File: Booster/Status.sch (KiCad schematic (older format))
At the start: 33 parts, among them J601 StatusLED, P601 ~OVERCURRENT_OUT, P602 ~OVERCURRENT_OUT_OP, P603 MSTR_SW, P604 MSTR_SW_OUT, P605 MSTR_SW_OUT_OP, P606 DRIVER_ENABLE_OUT_OP, P607 DRIVER_ENABLE_OUT, Q604 BC817-40, SW601 MSTR_SW, U601 74HC00, U602 PC817, U603 PC817, U604 PC817

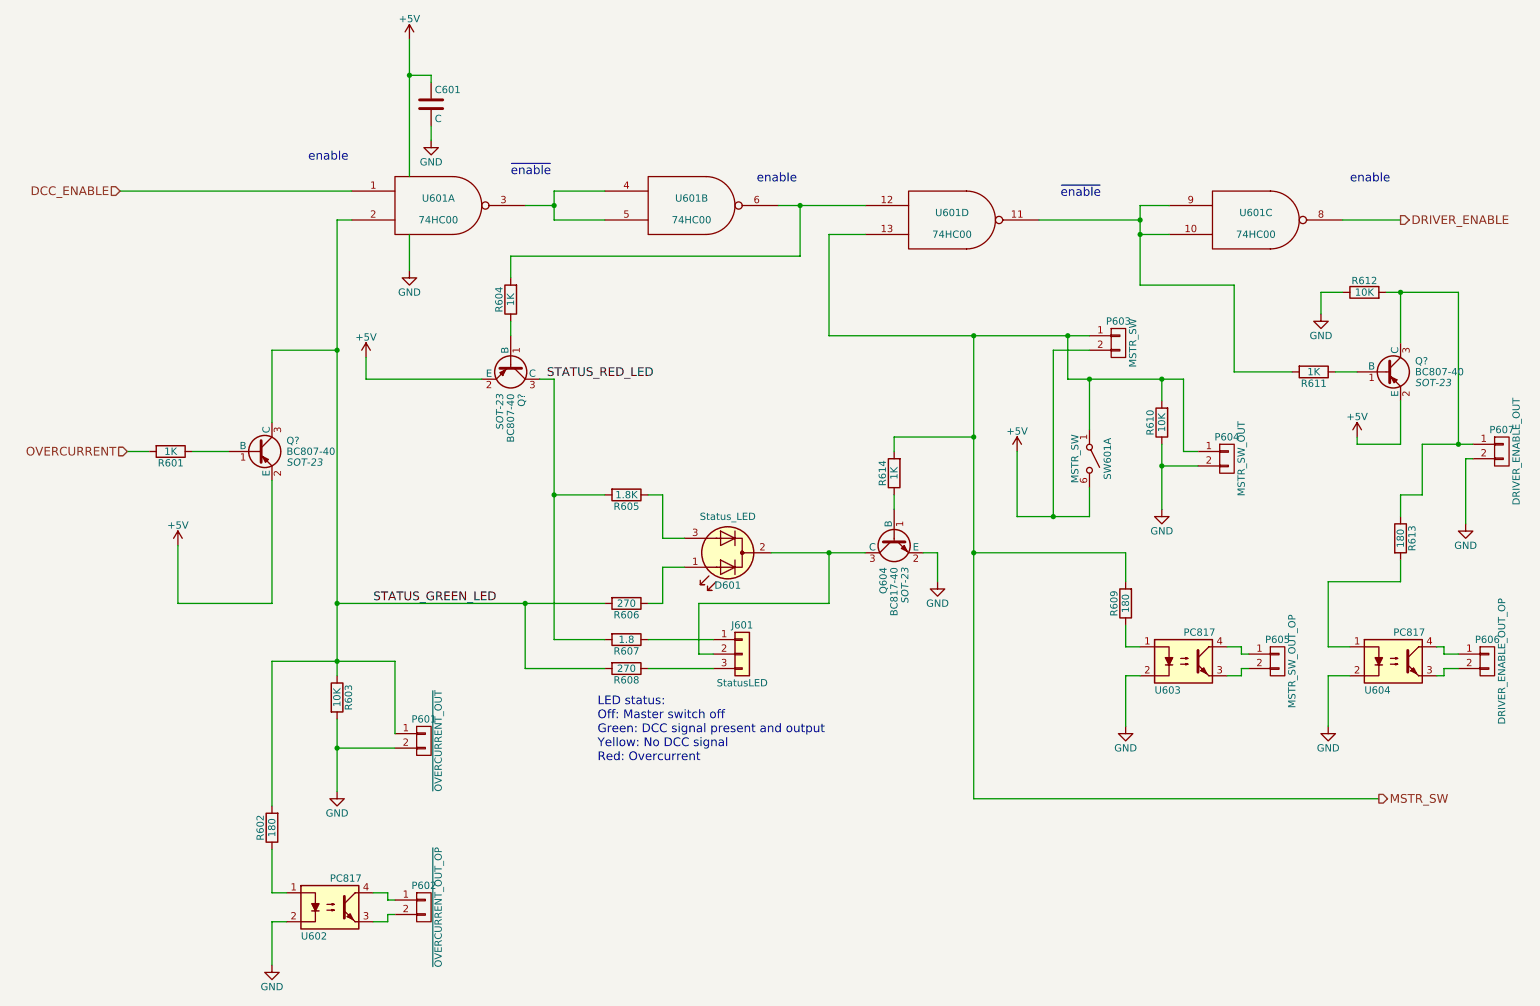
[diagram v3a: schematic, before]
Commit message: Replaced NAND gate with AND as the additional NOT gates ended up only used to negate the NAND gates directly. One extra AND gate used to allow resetting overcurrent by either master switch or DCC disable/enable.
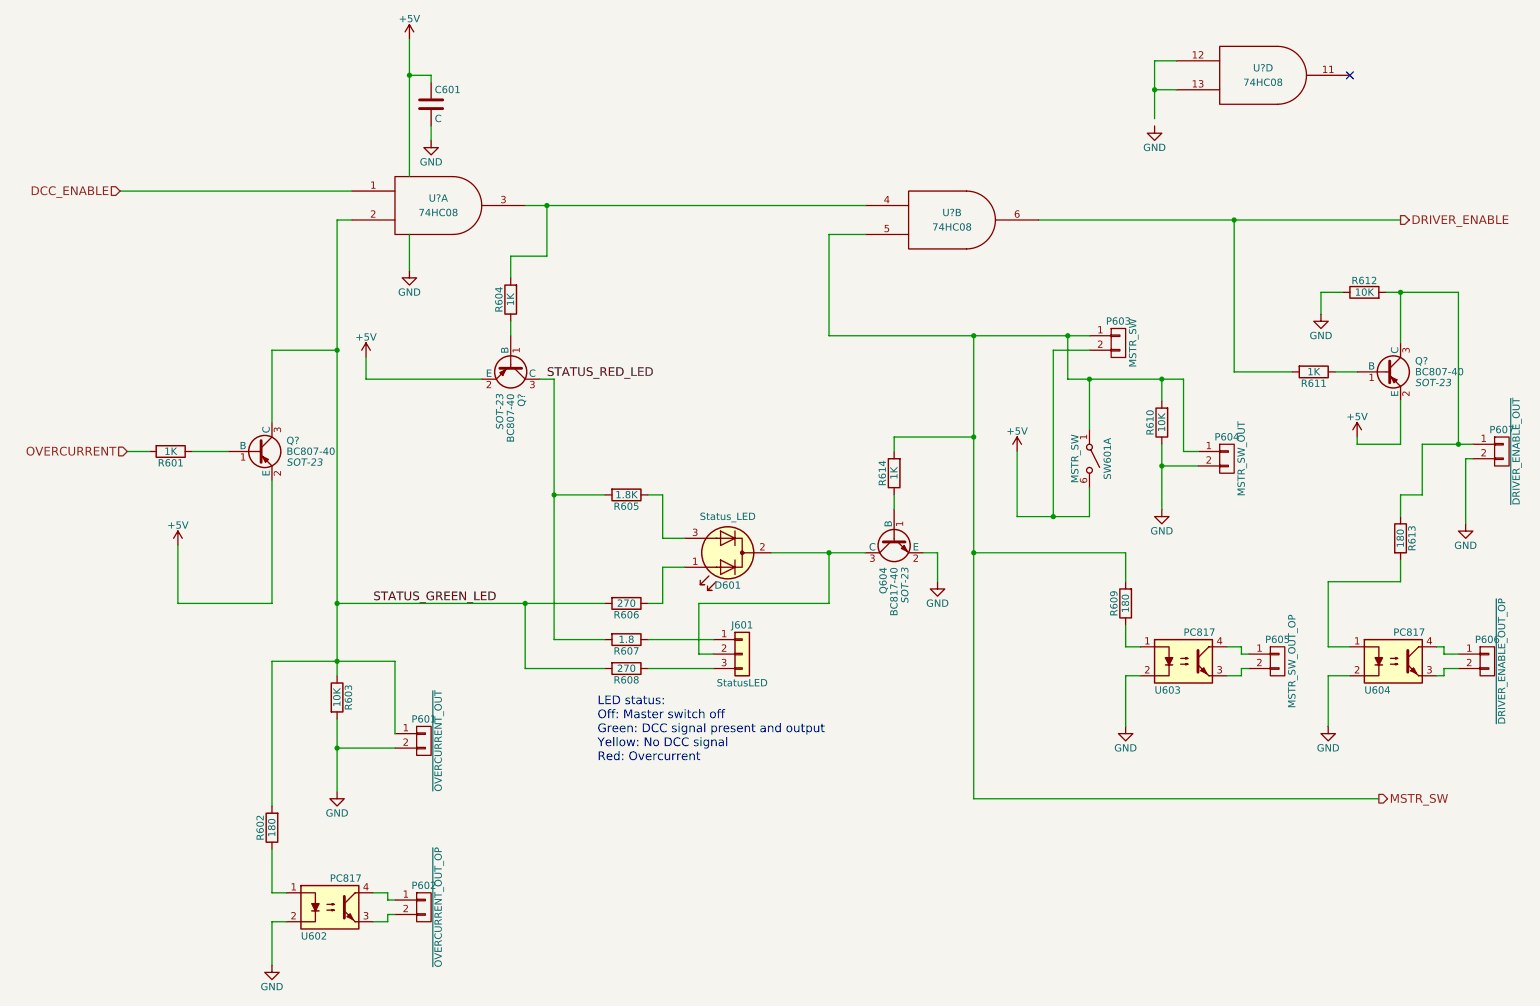
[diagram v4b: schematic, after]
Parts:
- removed U601: 74HC00, symbol 74HC00
- added U? (x3): 74HC08, symbol 74LS08
- P606: value DRIVER_ENABLE_OUT_OP -> ~DRIVER_ENABLE_OUT_OP
- P607: value DRIVER_ENABLE_OUT -> ~DRIVER_ENABLE_OUT
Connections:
- net +5V: now also U?.14 (VCC), U?.14 (VCC), U?.14 (VCC)
- net DCC_ENABLE: now also U?.1
- net DRIVER_ENABLE: now also R611.2, U?.6
- net GND: now also U?.7 (GND), U?.7 (GND), U?.7 (GND)
- net MSTR_SW: now also U?.5
- net STATUS_GREEN_LED: now also U?.2
- net at R604.2: now also U?.3, U?.4
- new net: U?.12, U?.13
- no-connect marks 0 -> 1
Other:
- note removed: "enable"
- note removed: "~enable"
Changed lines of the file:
@@
 P 10950 3650
 F 0 "P607" H 10950 3800 50  0000 C CNN
-F 1 "DRIVER_ENABLE_OUT" V 11050 3650 50  0000 C CNN
+F 1 "~DRIVER_ENABLE_OUT" V 11050 3650 50  0000 C CNN
 F 2 "" H 10950 3650 50  0000 C CNN
 F 3 "" H 10950 3650 50  0000 C CNN
@@
 P 10850 5100
 F 0 "P606" H 10850 5250 50  0000 C CNN
-F 1 "DRIVER_ENABLE_OUT_OP" V 10950 5100 50  0000 C CNN
+F 1 "~DRIVER_ENABLE_OUT_OP" V 10950 5100 50  0000 C CNN
 F 2 "" H 10850 5100 50  0000 C CNN
 F 3 "" H 10850 5100 50  0000 C CNN
@@
 $EndComp
 $Comp
-L 74HC00 U601
-U 1 1 5A1153E8
-P 3600 1950
-F 0 "U601" H 3600 2000 50  0000 C CNN
-F 1 "74HC00" H 3600 1850 50  0000 C CNN
-F 2 "" H 3600 1950 50  0001 C CNN
-F 3 "" H 3600 1950 50  0001 C CNN
-	1    3600 1950
-	1    0    0    -1
-$EndComp
-$Comp
-L 74HC00 U601
-U 2 1 5A11F087
-P 5350 1950
-F 0 "U601" H 5350 2000 50  0000 C CNN
-F 1 "74HC00" H 5350 1850 50  0000 C CNN
-F 2 "" H 5350 1950 50  0001 C CNN
-F 3 "" H 5350 1950 50  0001 C CNN
-	2    5350 1950
-	1    0    0    -1
-$EndComp
-Text Notes 2700 1650 0    60   ~ 0
-enable
-Text Notes 4100 1750 0    60   ~ 0
-~enable
-Text Notes 5800 1800 0    60   ~ 0
-enable
-$Comp
 L +5V #PWR048
 U 1 1 5A13183F
@@
 $EndComp
 $Comp
-L 74HC00 U601
-U 4 1 5A1330DE
-P 7150 2050
-F 0 "U601" H 7150 2100 50  0000 C CNN
-F 1 "74HC00" H 7150 1950 50  0000 C CNN
-F 2 "" H 7150 2050 50  0001 C CNN
-F 3 "" H 7150 2050 50  0001 C CNN
-	4    7150 2050
-	1    0    0    -1
-$EndComp
-$Comp
-L 74HC00 U601
-U 3 1 5A13319F
-P 9250 2050
-F 0 "U601" H 9250 2100 50  0000 C CNN
-F 1 "74HC00" H 9250 1950 50  0000 C CNN
-F 2 "" H 9250 2050 50  0001 C CNN
-F 3 "" H 9250 2050 50  0001 C CNN
-	3    9250 2050
-	1    0    0    -1
-$EndComp
-$Comp
 L GND #PWR049
 U 1 1 5A1534F1
@@
 	8100 2950 7850 2950
 Wire Wire Line
-	7600 4100 8100 4100
+	7600 4100 7850 4100
+Wire Wire Line
+	7850 4100 8100 4100
 Wire Wire Line
 	8100 4100 8100 3900
 Wire Wire Line
-	7950 3150 8750 3150
+	7950 3150 8100 3150
+Wire Wire Line
+	8100 3150 8600 3150
+Wire Wire Line
+	8600 3150 8750 3150
 Wire Wire Line
 	7950 2850 7950 3150
@@
 	5150 4450 5300 4450
 Wire Wire Line
-	4400 3150 4400 4950
+	4400 3150 4400 3950
+Wire Wire Line
+	4400 3950 4400 4950
 Wire Wire Line
 	4400 4950 4750 4950
@@
 	7850 2950 7850 4100
 Wire Wire Line
-	6300 2850 8100 2850
+	6300 2850 7300 2850
+Wire Wire Line
+	7300 2850 7950 2850
+Wire Wire Line
+	7950 2850 8100 2850
 Connection ~ 7850 4100
 Wire Wire Line
@@
 	10250 2900 10250 2550
 Wire Wire Line
-	10150 2550 10650 2550
+	10150 2550 10250 2550
+Wire Wire Line
+	10250 2550 10650 2550
 Wire Wire Line
 	10650 2550 10650 3600
 Wire Wire Line
-	10400 3600 10750 3600
+	10400 3600 10650 3600
+Wire Wire Line
+	10650 3600 10750 3600
 Wire Wire Line
 	10250 3600 9950 3600
@@
 	9700 2550 9700 2700
 Wire Wire Line
-	2900 2050 2900 5200
+	2900 2050 2900 2950
+Wire Wire Line
+	2900 2950 2900 4700
+Wire Wire Line
+	2900 4700 2900 5100
+Wire Wire Line
+	2900 5100 2900 5200
 Connection ~ 2900 4700
 Wire Wire Line
-	2900 5500 2900 6000
-Wire Wire Line
-	8600 3600 8600 4050
+	2900 5500 2900 5700
+Wire Wire Line
+	2900 5700 2900 6000
+Wire Wire Line
+	8600 3600 8600 3750
+Wire Wire Line
+	8600 3750 8600 4050
 Wire Wire Line
 	8600 3150 8600 3300
 Wire Wire Line
-	9500 3100 9100 3100
+	9100 3100 9500 3100
 Wire Wire Line
 	8750 3150 8750 3650
@@
 	3300 5100 3300 5600
 Wire Wire Line
-	2450 5100 3300 5100
+	2450 5100 2900 5100
+Wire Wire Line
+	2900 5100 3300 5100
 Connection ~ 2900 5100
 Wire Wire Line
@@
 	2900 2050 3000 2050
 Wire Wire Line
-	4200 1950 4400 1950
-Wire Wire Line
-	4400 1850 4750 1850
-Wire Wire Line
-	4400 2050 4750 2050
-Connection ~ 4400 1950
-Wire Wire Line
-	7750 2050 8450 2050
-Wire Wire Line
-	8450 1950 8450 2500
-Wire Wire Line
-	8450 1950 8650 1950
-Wire Wire Line
-	8450 2150 8650 2150
-Connection ~ 8450 2050
-Wire Wire Line
-	8450 2500 9100 2500
-Wire Wire Line
-	9100 2500 9100 3100
-Connection ~ 8450 2150
-Wire Wire Line
-	5950 1950 6550 1950
+	7750 2050 9100 2050
+Wire Wire Line
+	9100 2050 10250 2050
+Wire Wire Line
+	9100 2050 9100 3100
+Connection ~ 9100 2050
+Wire Wire Line
+	4200 1950 4350 1950
+Wire Wire Line
+	4350 1950 6550 1950
 Wire Wire Line
 	3900 3150 3100 3150
@@
 	4400 3950 4750 3950
 Wire Wire Line
-	9850 2050 10250 2050
-Wire Wire Line
 	3400 2150 3400 2400
 Wire Wire Line
-	3400 800  3400 1750
+	3400 800  3400 1050
+Wire Wire Line
+	3400 1050 3400 1750
 Wire Wire Line
 	3400 1050 3550 1050
@@
 	3550 1400 3550 1500
 Wire Wire Line
-	4400 1850 4400 2050
-Wire Wire Line
 	4100 2450 4100 2300
 Wire Wire Line
-	4100 2300 6100 2300
-Wire Wire Line
-	6100 2300 6100 1950
-Connection ~ 6100 1950
-Wire Wire Line
-	7300 2850 7300 6050
+	4100 2300 4350 2300
+Wire Wire Line
+	4350 2300 4350 1950
+Connection ~ 4350 1950
+Wire Wire Line
+	7300 2850 7300 3550
+Wire Wire Line
+	7300 3550 7300 4350
+Wire Wire Line
+	7300 4350 7300 6050
 Wire Wire Line
 	7300 6050 10100 6050
@@
 Wire Wire Line
 	1400 1850 3000 1850
-Text Notes 7900 1900 0    60   ~ 0
-~enable
-Text Notes 9900 1800 0    60   ~ 0
-enable
-Wire Wire Line
-	2900 4700 4750 4700
+Wire Wire Line
+	2900 4700 4200 4700
+Wire Wire Line
+	4200 4700 4750 4700
 Wire Wire Line
 	2450 2950 2900 2950
@@
 	6300 4700 6300 4350
 Wire Wire Line
-	5900 4350 6550 4350
+	5900 4350 6300 4350
+Wire Wire Line
+	6300 4350 6550 4350
 Wire Wire Line
 	6750 3950 6750 4050
@@
 Wire Wire Line
 	7050 4350 7050 4550
-$Comp
-L BC807-40 Q?
-U 1 1 5A3E8EA3
-P 10150 3100
-F 0 "Q?" H 10350 3175 50  0000 L CNN
-F 1 "BC807-40" H 10350 3100 50  0000 L CNN
-F 2 "SOT-23" H 10350 3025 50  0000 L CIN
-F 3 "" H 10150 3100 50  0000 L CNN
-	1    10150 3100
-	1    0    0    -1
-$EndComp
 $Comp
 L BC807-40 Q?
@@
 	1    0    0    -1
 $EndComp
+$Comp
+L 74LS08 U?
+U 1 1 5A3EB021
+P 3600 1950
+F 0 "U?" H 3600 2000 50  0000 C CNN
+F 1 "74HC08" H 3600 1900 50  0000 C CNN
+F 2 "" H 3600 1950 50  0000 C CNN
+F 3 "" H 3600 1950 50  0000 C CNN
+	1    3600 1950
+	1    0    0    -1
+$EndComp
+$Comp
+L BC807-40 Q?
+U 1 1 5A3E8EA3
+P 10150 3100
+F 0 "Q?" H 10350 3175 50  0000 L CNN
+F 1 "BC807-40" H 10350 3100 50  0000 L CNN
+F 2 "SOT-23" H 10350 3025 50  0000 L CIN
+F 3 "" H 10150 3100 50  0000 L CNN
+	1    10150 3100
+	1    0    0    -1
+$EndComp
+$Comp
+L 74LS08 U?
+U 2 1 5A3EB62D
+P 7150 2050
+F 0 "U?" H 7150 2100 50  0000 C CNN
+F 1 "74HC08" H 7150 2000 50  0000 C CNN
+F 2 "" H 7150 2050 50  0000 C CNN
+F 3 "" H 7150 2050 50  0000 C CNN
+	2    7150 2050
+	1    0    0    -1
+$EndComp
+$Comp
+L 74LS08 U?
+U 4 1 5A3F64C1
+P 9300 1050
+F 0 "U?" H 9300 1100 50  0000 C CNN
+F 1 "74HC08" H 9300 1000 50  0000 C CNN
+F 2 "" H 9300 1050 50  0000 C CNN
+F 3 "" H 9300 1050 50  0000 C CNN
+	4    9300 1050
+	1    0    0    -1
+$EndComp
+NoConn ~ 9900 1050
+Wire Wire Line
+	8700 950  8550 950
+Wire Wire Line
+	8550 950  8550 1150
+Wire Wire Line
+	8550 1150 8550 1350
+Wire Wire Line
+	8700 1150 8550 1150
+Connection ~ 8550 1150
+$Comp
+L GND #PWR?
+U 1 1 5A3F671E
+P 8550 1400
+F 0 "#PWR?" H 8550 1150 50  0001 C CNN
+F 1 "GND" H 8550 1250 50  0000 C CNN
+F 2 "" H 8550 1400 50  0000 C CNN
+F 3 "" H 8550 1400 50  0000 C CNN
+	1    8550 1400
+	1    0    0    -1
+$EndComp

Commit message: Annotation, fix missing connection.
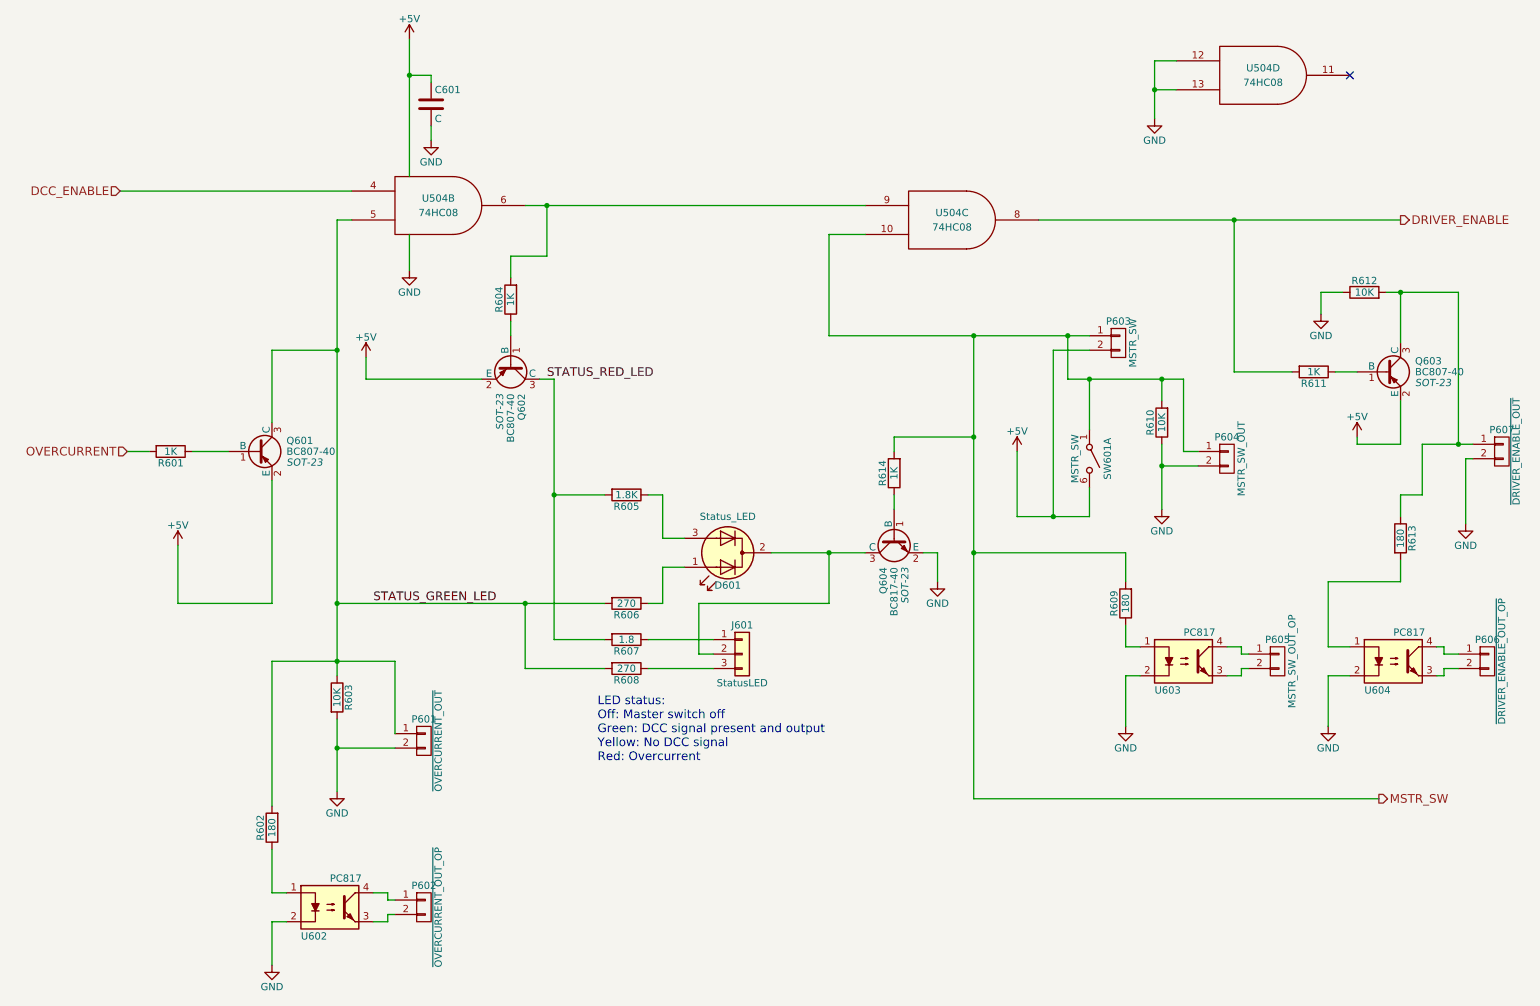
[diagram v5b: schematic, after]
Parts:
- gave numbers to parts that had none: 4
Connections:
- net DCC_ENABLE: now also U504.4; no longer U504.1
- net DRIVER_ENABLE: now also U504.8; no longer U504.6
- net GND: now also U504.12, U504.13
- net MSTR_SW: now also U504.10; no longer U504.5
- net STATUS_GREEN_LED: now also U504.5; no longer U504.2
- new net: R604.2, U504.6, U504.9
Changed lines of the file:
@@
 	8100 2950 7850 2950
 Wire Wire Line
-	7600 4100 7850 4100
-Wire Wire Line
-	7850 4100 8100 4100
+	7600 4100 8100 4100
 Wire Wire Line
 	8100 4100 8100 3900
 Wire Wire Line
-	7950 3150 8100 3150
-Wire Wire Line
-	8100 3150 8600 3150
-Wire Wire Line
-	8600 3150 8750 3150
+	7950 3150 8750 3150
 Wire Wire Line
 	7950 2850 7950 3150
@@
 	5150 4450 5300 4450
 Wire Wire Line
-	4400 3150 4400 3950
-Wire Wire Line
-	4400 3950 4400 4950
+	4400 3150 4400 4950
 Wire Wire Line
 	4400 4950 4750 4950
@@
 	7850 2950 7850 4100
 Wire Wire Line
-	6300 2850 7300 2850
-Wire Wire Line
-	7300 2850 7950 2850
-Wire Wire Line
-	7950 2850 8100 2850
+	6300 2850 8100 2850
 Connection ~ 7850 4100
 Wire Wire Line
@@
 	10250 2900 10250 2550
 Wire Wire Line
-	10150 2550 10250 2550
-Wire Wire Line
-	10250 2550 10650 2550
+	10150 2550 10650 2550
 Wire Wire Line
 	10650 2550 10650 3600
 Wire Wire Line
-	10400 3600 10650 3600
-Wire Wire Line
-	10650 3600 10750 3600
+	10400 3600 10750 3600
 Wire Wire Line
 	10250 3600 9950 3600
@@
 	9700 2550 9700 2700
 Wire Wire Line
-	2900 2050 2900 2950
-Wire Wire Line
-	2900 2950 2900 4700
-Wire Wire Line
-	2900 4700 2900 5100
-Wire Wire Line
-	2900 5100 2900 5200
+	2900 2050 2900 5200
 Connection ~ 2900 4700
 Wire Wire Line
-	2900 5500 2900 5700
-Wire Wire Line
-	2900 5700 2900 6000
-Wire Wire Line
-	8600 3600 8600 3750
-Wire Wire Line
-	8600 3750 8600 4050
+	2900 5500 2900 6000
+Wire Wire Line
+	8600 3600 8600 4050
 Wire Wire Line
 	8600 3150 8600 3300
@@
 	3300 5100 3300 5600
 Wire Wire Line
-	2450 5100 2900 5100
-Wire Wire Line
-	2900 5100 3300 5100
+	2450 5100 3300 5100
 Connection ~ 2900 5100
 Wire Wire Line
@@
 	2900 2050 3000 2050
 Wire Wire Line
-	7750 2050 9100 2050
-Wire Wire Line
-	9100 2050 10250 2050
+	7750 2050 10250 2050
 Wire Wire Line
 	9100 2050 9100 3100
 Connection ~ 9100 2050
 Wire Wire Line
-	4200 1950 4350 1950
-Wire Wire Line
-	4350 1950 6550 1950
+	4200 1950 6550 1950
 Wire Wire Line
 	3900 3150 3100 3150
@@
 	3400 2150 3400 2400
 Wire Wire Line
-	3400 800  3400 1050
-Wire Wire Line
-	3400 1050 3400 1750
+	3400 800  3400 1750
 Wire Wire Line
 	3400 1050 3550 1050
@@
 Connection ~ 4350 1950
 Wire Wire Line
-	7300 2850 7300 3550
-Wire Wire Line
-	7300 3550 7300 4350
-Wire Wire Line
-	7300 4350 7300 6050
+	7300 2850 7300 6050
 Wire Wire Line
 	7300 6050 10100 6050
@@
 	1400 1850 3000 1850
 Wire Wire Line
-	2900 4700 4200 4700
-Wire Wire Line
-	4200 4700 4750 4700
+	2900 4700 4750 4700
 Wire Wire Line
 	2450 2950 2900 2950
@@
 	6300 4700 6300 4350
 Wire Wire Line
-	5900 4350 6300 4350
-Wire Wire Line
-	6300 4350 6550 4350
+	5900 4350 6550 4350
 Wire Wire Line
 	6750 3950 6750 4050
@@
 	7050 4350 7050 4550
 $Comp
-L BC807-40 Q?
+L BC807-40 Q602
 U 1 1 5A3E9138
 P 4100 3050
-F 0 "Q?" H 4300 3125 50  0000 L CNN
+F 0 "Q602" H 4300 3125 50  0000 L CNN
 F 1 "BC807-40" H 4300 3050 50  0000 L CNN
 F 2 "SOT-23" H 4300 2975 50  0000 L CIN
@@
 $EndComp
 $Comp
-L BC807-40 Q?
+L BC807-40 Q601
 U 1 1 5A3E9B01
 P 2350 3650
-F 0 "Q?" H 2550 3725 50  0000 L CNN
+F 0 "Q601" H 2550 3725 50  0000 L CNN
 F 1 "BC807-40" H 2550 3650 50  0000 L CNN
 F 2 "SOT-23" H 2550 3575 50  0000 L CIN
@@
 $EndComp
 $Comp
-L 74LS08 U?
-U 1 1 5A3EB021
+L 74LS08 U504
+U 2 1 5A3EB021
 P 3600 1950
-F 0 "U?" H 3600 2000 50  0000 C CNN
+F 0 "U504" H 3600 2000 50  0000 C CNN
 F 1 "74HC08" H 3600 1900 50  0000 C CNN
 F 2 "" H 3600 1950 50  0000 C CNN
 F 3 "" H 3600 1950 50  0000 C CNN
-	1    3600 1950
-	1    0    0    -1
-$EndComp
-$Comp
-L BC807-40 Q?
+	2    3600 1950
+	1    0    0    -1
+$EndComp
+$Comp
+L BC807-40 Q603
 U 1 1 5A3E8EA3
 P 10150 3100
-F 0 "Q?" H 10350 3175 50  0000 L CNN
+F 0 "Q603" H 10350 3175 50  0000 L CNN
 F 1 "BC807-40" H 10350 3100 50  0000 L CNN
 F 2 "SOT-23" H 10350 3025 50  0000 L CIN
@@
 $EndComp
 $Comp
-L 74LS08 U?
-U 2 1 5A3EB62D
+L 74LS08 U504
+U 3 1 5A3EB62D
 P 7150 2050
-F 0 "U?" H 7150 2100 50  0000 C CNN
+F 0 "U504" H 7150 2100 50  0000 C CNN
 F 1 "74HC08" H 7150 2000 50  0000 C CNN
 F 2 "" H 7150 2050 50  0000 C CNN
 F 3 "" H 7150 2050 50  0000 C CNN
-	2    7150 2050
-	1    0    0    -1
-$EndComp
-$Comp
-L 74LS08 U?
+	3    7150 2050
+	1    0    0    -1
+$EndComp
+$Comp
+L 74LS08 U504
 U 4 1 5A3F64C1
 P 9300 1050
-F 0 "U?" H 9300 1100 50  0000 C CNN
+F 0 "U504" H 9300 1100 50  0000 C CNN
 F 1 "74HC08" H 9300 1000 50  0000 C CNN
 F 2 "" H 9300 1050 50  0000 C CNN
@@
 	8700 950  8550 950
 Wire Wire Line
-	8550 950  8550 1150
-Wire Wire Line
-	8550 1150 8550 1350
+	8550 950  8550 1350
 Wire Wire Line
 	8700 1150 8550 1150
 Connection ~ 8550 1150
 $Comp
-L GND #PWR?
+L GND #PWR053
 U 1 1 5A3F671E
-P 8550 1400
-F 0 "#PWR?" H 8550 1150 50  0001 C CNN
-F 1 "GND" H 8550 1250 50  0000 C CNN
-F 2 "" H 8550 1400 50  0000 C CNN
-F 3 "" H 8550 1400 50  0000 C CNN
-	1    8550 1400
-	1    0    0    -1
-$EndComp
+P 8550 1350
+F 0 "#PWR053" H 8550 1100 50  0001 C CNN
+F 1 "GND" H 8550 1200 50  0000 C CNN
+F 2 "" H 8550 1350 50  0000 C CNN
+F 3 "" H 8550 1350 50  0000 C CNN
+	1    8550 1350
+	1    0    0    -1
+$EndComp
